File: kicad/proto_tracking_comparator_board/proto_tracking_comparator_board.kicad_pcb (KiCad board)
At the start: 2 copper layers, 17 x 13.5 mm, 19 parts, among them U1 TLV3542, U2 MCP6566

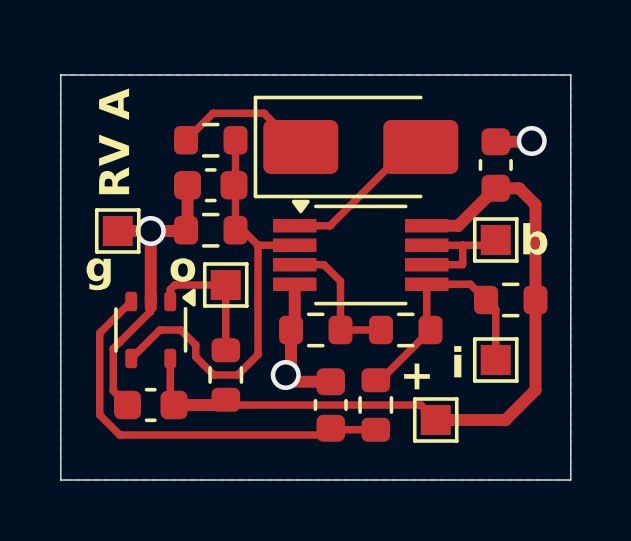
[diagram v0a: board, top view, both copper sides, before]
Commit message: Save bodge board rev B and additional sims
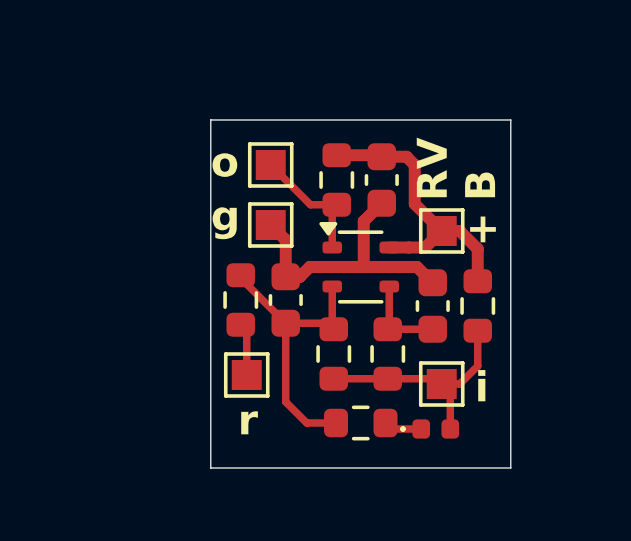
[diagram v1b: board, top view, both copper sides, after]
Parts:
- removed the C1 at (58.5, 16.0)
- removed the R2 at (55.5, 21.5)
- removed the R3 at (52.5, 21.5)
- removed the R5 at (49.0, 18.2)
- removed the U1 at (54.0, 19.0)
- added R1: 100k, Resistor_SMD:R_0603_1608Metric, F.Cu at (53.1, 22.3)
- added R6: 1M, Resistor_SMD:R_0603_1608Metric, F.Cu at (50.0, 20.5)
- C2: value 1nF -> 100pF
- C3: value DNP -> 3pF
- D1: footprint Diode_SMD:D_SMA -> Custom_Diode:D_0402_1005Metric
- R4: value 1k -> 10k
- R5: renamed from R6; value 0R -> 10k
- moved C1 10.7 mm to (54.7, 16.5), turned to 90 degrees
- moved R4 10.7 mm to (54.0, 24.6), turned to 180 degrees
- moved D1 9.73 mm to (56.5, 24.8)
- moved TP5 9.44 mm to (50.2, 23.0)
- moved R3 7.48 mm to (53.2, 16.5), turned to -90 degrees
- moved U1 7.31 mm to (54.0, 19.4), turned to 0 degrees
- moved TP3 6.30 mm to (56.7, 18.2)
- moved TP4 5.10 mm to (51.0, 18.0)
- moved C3 4.74 mm to (56.4, 20.7)
- moved C2 4.57 mm to (51.5, 20.5), turned to 90 degrees
- moved TP2 4.27 mm to (51.0, 16.0)
- moved TP1 1.97 mm to (56.7, 23.3)
- moved R5 1.75 mm to (54.9, 22.3), turned to 90 degrees
- moved R2 1.12 mm to (57.9, 20.7), turned to -90 degrees
- renumbered C4 to C1, R1 to R2, R7 to R3, U2 to U1
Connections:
- C2 pad 1: /PEAK -> Net-(U1-+)
- C3 pad 1: Net-(U2-+) -> Net-(U1--)
- D1 pad 2: Net-(D1-A) -> /RF_DET_OUT
- R4 pad 2: /PEAK -> Net-(U1-+)
- R5 pad 2: Net-(U2-+) -> Net-(U1--)
- TP5 pad 1: /BUF -> /RSSI
- U1 pad 3: Net-(U2-+) -> Net-(U1-+)
- U1 pad 4: /PEAK -> Net-(U1--)
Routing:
- net +3V3: track 25.0 -> 9.81 mm
- net /PEAK: track 14.6 -> 0.00 mm
- net Net-(U2-+): track 13.8 -> 0.00 mm
- net Net-(U1-+): track 0.00 -> 9.94 mm
- net GND: track 16.3 -> 9.56 mm, vias 3 -> 0
- net Net-(D1-A): track 5.25 -> 0.00 mm
- net Net-(U1A-+): track 4.73 -> 0.00 mm
- net /BUF: track 4.21 -> 0.00 mm
- net Net-(D1-K): track 4.71 -> 1.27 mm
- net Net-(U1--): track 0.00 -> 2.95 mm
- net /RSSI: track 0.00 -> 1.76 mm
- net /RF_DET_OUT: track 8.42 -> 7.91 mm
- removed copper zone on B.Cu, net GND
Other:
- board size 17 x 13.5 mm -> 10 x 11.6 mm
- board text added: "RV B"
- board text added: "r"
- board text removed: "RV A"
- board text removed: "b"

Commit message: Data slicer rev A
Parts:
- removed C2: 100pF, Capacitor_SMD:C_0603_1608Metric
- removed R3: 1k, Resistor_SMD:R_0603_1608Metric
- removed R4: 10k, Resistor_SMD:R_0603_1608Metric
- removed R6: 1M, Resistor_SMD:R_0603_1608Metric
- removed TP3: TestPoint, TestPoint:TestPoint_Pad_1.0x1.0mm
- removed U1: MCP6566, Package_TO_SOT_SMD:SOT-353_SC-70-5
- added D2: D_Schottky, Custom_Diode:D_0402_1005Metric, F.Cu at (25.0, 19.0)
- added R7: 200k, Resistor_SMD:R_0603_1608Metric, F.Cu at (30.5, 19.5)
- added TP6: TestPoint, TestPoint:TestPoint_Pad_1.0x1.0mm, F.Cu at (32.5, 16.0)
- added TP7: TestPoint, TestPoint:TestPoint_Pad_1.0x1.0mm, F.Cu at (32.5, 18.0)
- C3: value 3pF -> 1nF
- R1: value 100k -> 10k
- R2: value 1k -> 100k
- R5: value 10k -> 100k
- moved TP1 34.6 mm to (22.5, 18.0)
- moved D1 32.3 mm to (25.0, 17.5), turned to 180 degrees
- moved TP2 28.9 mm to (22.5, 20.5)
- moved TP5 28.6 mm to (22.5, 15.8)
- moved C3 28.5 mm to (28.0, 19.0), turned to 0 degrees
- moved R1 28.2 mm to (25.0, 20.5), turned to 180 degrees
- moved R2 27.7 mm to (30.5, 16.5), turned to 90 degrees
- moved R5 27.3 mm to (28.0, 17.5), turned to 180 degrees
- moved C1 27.0 mm to (28.0, 20.5), turned to 0 degrees
- moved TP4 18.6 mm to (32.5, 20.3)
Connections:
- C1 pad 1: GND -> Net-(D2-A)
- C1 pad 2: +3V3 -> GND
- C3 pad 1: Net-(U1--) -> /RSSI
- D1 pad 1: Net-(D1-K) -> /RSSI
- D1 pad 2: /RF_DET_OUT -> /RF_LEVEL
- R1 pad 1: /RF_DET_OUT -> Net-(D2-A)
- R1 pad 2: Net-(U1-+) -> /TL_FLOOR
- R2 pad 1: +3V3 -> /TL_LO
- R2 pad 2: /RF_DET_OUT -> /TL_HI
- R5 pad 1: /RF_DET_OUT -> /TL_HI
- R5 pad 2: Net-(U1--) -> /RSSI
- TP1 pad 1: /RF_DET_OUT -> /RF_LEVEL
- TP2 pad 1: /PULSES -> /TL_FLOOR
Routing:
- net Net-(U1-+): track 9.94 -> 0.00 mm
- net +3V3: track 9.81 -> 0.00 mm
- net /RF_DET_OUT: track 7.91 -> 0.00 mm
- net /RSSI: track 1.76 -> 8.70 mm
- net /TL_HI: track 0.00 -> 4.65 mm
- net GND: track 9.56 -> 5.31 mm
- net /PULSES: track 4.24 -> 0.00 mm
- net Net-(D2-A): track 0.00 -> 3.44 mm
- net /TL_LO: track 0.00 -> 3.35 mm
- net Net-(U1--): track 2.95 -> 0.00 mm
- net /RF_LEVEL: track 0.00 -> 2.22 mm
- net /TL_FLOOR: track 0.00 -> 1.68 mm
- net Net-(D1-K): track 1.27 -> 0.00 mm
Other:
- board size 10 x 11.6 mm -> 17 x 7.5 mm
- board text added: "RV C"
- board text added: "rl"
- board text added: "rs"
- board text added: "tf"
- board text added: "th"
- board text added: "tl"
- board text removed: "+"
- board text removed: "RV B"
- board text removed: "i"
- board text removed: "o"
- board text removed: "r"
